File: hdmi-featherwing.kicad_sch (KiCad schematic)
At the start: 10 parts, among them J1 HDMI_A

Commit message: route diffpairs
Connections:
- net WING_CK+: now also A1.20 (D1); no longer A1.10 (A5)
- net WING_CK-: now also A1.19 (D0); no longer A1.9 (A4)
- net WING_D0+: now also A1.22 (D3); no longer A1.24 (D5)
- net WING_D0-: now also A1.21 (D2); no longer A1.23 (D4)
- net WING_D1+: now also A1.24 (D5); no longer A1.22 (D3)
- net WING_D1-: now also A1.23 (D4); no longer A1.21 (D2)
- net WING_D2+: now also A1.10 (A5); no longer A1.20 (D1)
- net WING_D2-: now also A1.9 (A4); no longer A1.19 (D0)
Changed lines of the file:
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@@
     (stroke (width 0) (type solid) (color 0 0 0 0))
   )
-  (label "WING_D2-" (at 97.79 62.865 180)
+  (label "WING_CK-" (at 97.79 62.865 180)
     (effects (font (size 1.27 1.27)) (justify right bottom))
   )
-  (label "WING_D2+" (at 97.79 65.405 180)
+  (label "WING_CK+" (at 97.79 65.405 180)
     (effects (font (size 1.27 1.27)) (justify right bottom))
   )
-  (label "WING_D1-" (at 97.79 67.945 180)
+  (label "WING_D0-" (at 97.79 67.945 180)
     (effects (font (size 1.27 1.27)) (justify right bottom))
   )
-  (label "WING_D1+" (at 97.79 70.485 180)
+  (label "WING_D0+" (at 97.79 70.485 180)
     (effects (font (size 1.27 1.27)) (justify right bottom))
   )
-  (label "WING_D0-" (at 97.79 73.025 180)
+  (label "WING_D1-" (at 97.79 73.025 180)
     (effects (font (size 1.27 1.27)) (justify right bottom))
   )
-  (label "WING_D0+" (at 97.79 75.565 180)
+  (label "WING_D1+" (at 97.79 75.565 180)
     (effects (font (size 1.27 1.27)) (justify right bottom))
   )
-  (label "WING_CK-" (at 123.19 88.265 0)
+  (label "WING_D2-" (at 123.19 88.265 0)
     (effects (font (size 1.27 1.27)) (justify left bottom))
   )
-  (label "WING_CK+" (at 123.19 90.805 0)
+  (label "WING_D2+" (at 123.19 90.805 0)
     (effects (font (size 1.27 1.27)) (justify left bottom))
   )

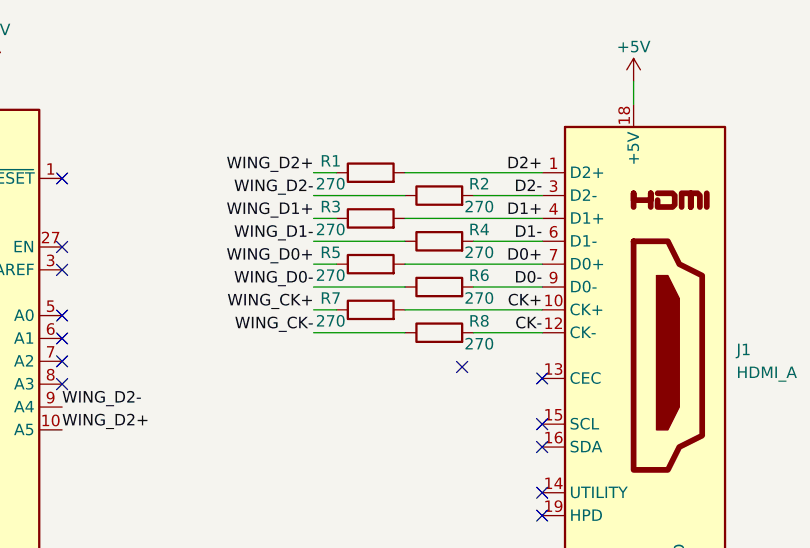
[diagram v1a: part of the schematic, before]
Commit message: 300 ohm resistors
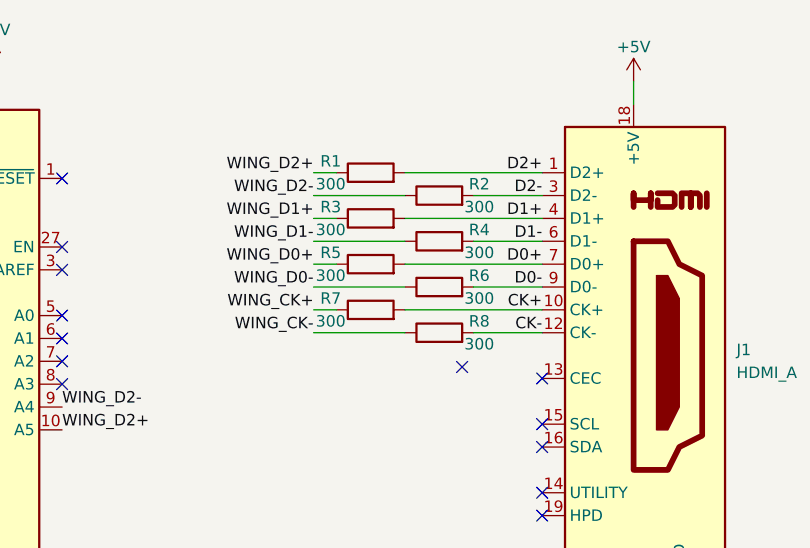
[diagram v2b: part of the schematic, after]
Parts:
- R1, R2, R3, R4, R5, R6, R7, R8: value 270 -> 300
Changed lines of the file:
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@@
     (in_bom yes) (on_board yes)
     (property "Reference" "R1" (id 0) (at 153.035 60.96 90))
-    (property "Value" "270" (id 1) (at 153.035 63.5 90))
+    (property "Value" "300" (id 1) (at 153.035 63.5 90))
     (property "Footprint" "Resistor_SMD:R_0402_1005Metric" (id 2) (at 157.48 64.008 90)
       (effects (font (size 1.27 1.27)) hide)
@@
     (in_bom yes) (on_board yes)
     (property "Reference" "R3" (id 0) (at 153.035 66.04 90))
-    (property "Value" "270" (id 1) (at 153.035 68.58 90))
+    (property "Value" "300" (id 1) (at 153.035 68.58 90))
     (property "Footprint" "Resistor_SMD:R_0402_1005Metric" (id 2) (at 157.48 69.088 90)
       (effects (font (size 1.27 1.27)) hide)
@@
     (in_bom yes) (on_board yes)
     (property "Reference" "R5" (id 0) (at 153.035 71.12 90))
-    (property "Value" "270" (id 1) (at 153.035 73.66 90))
+    (property "Value" "300" (id 1) (at 153.035 73.66 90))
     (property "Footprint" "Resistor_SMD:R_0402_1005Metric" (id 2) (at 157.48 74.168 90)
       (effects (font (size 1.27 1.27)) hide)
@@
     (in_bom yes) (on_board yes)
     (property "Reference" "R7" (id 0) (at 153.035 76.2 90))
-    (property "Value" "270" (id 1) (at 153.035 78.74 90))
+    (property "Value" "300" (id 1) (at 153.035 78.74 90))
     (property "Footprint" "Resistor_SMD:R_0402_1005Metric" (id 2) (at 157.48 79.248 90)
       (effects (font (size 1.27 1.27)) hide)
@@
     (in_bom yes) (on_board yes)
     (property "Reference" "R2" (id 0) (at 169.545 63.5 90))
-    (property "Value" "270" (id 1) (at 169.545 66.04 90))
+    (property "Value" "300" (id 1) (at 169.545 66.04 90))
     (property "Footprint" "Resistor_SMD:R_0402_1005Metric" (id 2) (at 165.1 66.548 90)
       (effects (font (size 1.27 1.27)) hide)
@@
     (in_bom yes) (on_board yes)
     (property "Reference" "R4" (id 0) (at 169.545 68.58 90))
-    (property "Value" "270" (id 1) (at 169.545 71.12 90))
+    (property "Value" "300" (id 1) (at 169.545 71.12 90))
     (property "Footprint" "Resistor_SMD:R_0402_1005Metric" (id 2) (at 165.1 71.628 90)
       (effects (font (size 1.27 1.27)) hide)
@@
     (in_bom yes) (on_board yes)
     (property "Reference" "R6" (id 0) (at 169.545 73.66 90))
-    (property "Value" "270" (id 1) (at 169.545 76.2 90))
+    (property "Value" "300" (id 1) (at 169.545 76.2 90))
     (property "Footprint" "Resistor_SMD:R_0402_1005Metric" (id 2) (at 165.1 76.708 90)
       (effects (font (size 1.27 1.27)) hide)
@@
     (in_bom yes) (on_board yes)
     (property "Reference" "R8" (id 0) (at 169.545 78.74 90))
-    (property "Value" "270" (id 1) (at 169.545 81.28 90))
+    (property "Value" "300" (id 1) (at 169.545 81.28 90))
     (property "Footprint" "Resistor_SMD:R_0402_1005Metric" (id 2) (at 165.1 81.788 90)
       (effects (font (size 1.27 1.27)) hide)
@@
     )
     (path "/12095942-e316-43e6-8e91-820591daa66e"
-      (reference "R1") (unit 1) (value "270") (footprint "Resistor_SMD:R_0402_1005Metric")
+      (reference "R1") (unit 1) (value "300") (footprint "Resistor_SMD:R_0402_1005Metric")
     )
     (path "/55298014-470c-4e6b-a6bd-6f35e8695295"
-      (reference "R2") (unit 1) (value "270") (footprint "Resistor_SMD:R_0402_1005Metric")
+      (reference "R2") (unit 1) (value "300") (footprint "Resistor_SMD:R_0402_1005Metric")
     )
     (path "/eeb927ea-8397-4c7d-9a56-27649363bfbf"
-      (reference "R3") (unit 1) (value "270") (footprint "Resistor_SMD:R_0402_1005Metric")
+      (reference "R3") (unit 1) (value "300") (footprint "Resistor_SMD:R_0402_1005Metric")
     )
     (path "/692d872f-84be-419d-83c1-adc9ca84bc76"
-      (reference "R4") (unit 1) (value "270") (footprint "Resistor_SMD:R_0402_1005Metric")
+      (reference "R4") (unit 1) (value "300") (footprint "Resistor_SMD:R_0402_1005Metric")
     )
     (path "/d3d37288-f0ba-4fe0-9fd0-56afc5bb6815"
-      (reference "R5") (unit 1) (value "270") (footprint "Resistor_SMD:R_0402_1005Metric")
+      (reference "R5") (unit 1) (value "300") (footprint "Resistor_SMD:R_0402_1005Metric")
     )
     (path "/1725c309-b4c5-44b0-b5f8-36484d1f71d5"
-      (reference "R6") (unit 1) (value "270") (footprint "Resistor_SMD:R_0402_1005Metric")
+      (reference "R6") (unit 1) (value "300") (footprint "Resistor_SMD:R_0402_1005Metric")
     )
     (path "/c8b38ce0-8172-4ca5-b311-7991ef2356c2"
-      (reference "R7") (unit 1) (value "270") (footprint "Resistor_SMD:R_0402_1005Metric")
+      (reference "R7") (unit 1) (value "300") (footprint "Resistor_SMD:R_0402_1005Metric")
     )
     (path "/f3c2cf24-508f-45aa-96e8-0cfa5e7c4c3d"
-      (reference "R8") (unit 1) (value "270") (footprint "Resistor_SMD:R_0402_1005Metric")
-    )
-  )
+      (reference "R8") (unit 1) (value "300") (footprint "Resistor_SMD:R_0402_1005Metric")
+    )
+  )

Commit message: Add LCSC property
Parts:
- R1, R2, R3, R4, R5, R6, R7, R8: LCSC (none) -> C25102
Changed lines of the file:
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@@
       (effects (font (size 1.27 1.27)) hide)
     )
-    (property "LCSC" "" (id 4) (at 157.48 62.23 90)
+    (property "LCSC" "C25102" (id 4) (at 157.48 62.23 90)
       (effects (font (size 1.27 1.27)) hide)
     )
@@
       (effects (font (size 1.27 1.27)) hide)
     )
-    (property "LCSC" "" (id 4) (at 157.48 67.31 90)
+    (property "LCSC" "C25102" (id 4) (at 157.48 67.31 90)
       (effects (font (size 1.27 1.27)) hide)
     )
@@
       (effects (font (size 1.27 1.27)) hide)
     )
-    (property "LCSC" "" (id 4) (at 157.48 72.39 90)
+    (property "LCSC" "C25102" (id 4) (at 157.48 72.39 90)
       (effects (font (size 1.27 1.27)) hide)
     )
@@
       (effects (font (size 1.27 1.27)) hide)
     )
-    (property "LCSC" "" (id 4) (at 157.48 77.47 90)
+    (property "LCSC" "C25102" (id 4) (at 157.48 77.47 90)
       (effects (font (size 1.27 1.27)) hide)
     )
@@
       (effects (font (size 1.27 1.27)) hide)
     )
-    (property "LCSC" "" (id 4) (at 165.1 64.77 90)
+    (property "LCSC" "C25102" (id 4) (at 165.1 64.77 90)
       (effects (font (size 1.27 1.27)) hide)
     )
@@
       (effects (font (size 1.27 1.27)) hide)
     )
-    (property "LCSC" "" (id 4) (at 165.1 69.85 90)
+    (property "LCSC" "C25102" (id 4) (at 165.1 69.85 90)
       (effects (font (size 1.27 1.27)) hide)
     )
@@
       (effects (font (size 1.27 1.27)) hide)
     )
-    (property "LCSC" "" (id 4) (at 165.1 74.93 90)
+    (property "LCSC" "C25102" (id 4) (at 165.1 74.93 90)
       (effects (font (size 1.27 1.27)) hide)
     )
@@
       (effects (font (size 1.27 1.27)) hide)
     )
-    (property "LCSC" "" (id 4) (at 165.1 80.01 90)
+    (property "LCSC" "C25102" (id 4) (at 165.1 80.01 90)
       (effects (font (size 1.27 1.27)) hide)
     )
